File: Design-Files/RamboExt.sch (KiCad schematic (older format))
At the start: 44 parts, among them K1 SEL_THERM_4, K2 SEL_THERM_3, K3 MS3_E2, K4 MS2_E2, K5 MS1_E2, K6 MS3_E3, K7 MS2_E3, K8 MS1_E3, P1 STEPPER_2, P2 STEPPER_3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

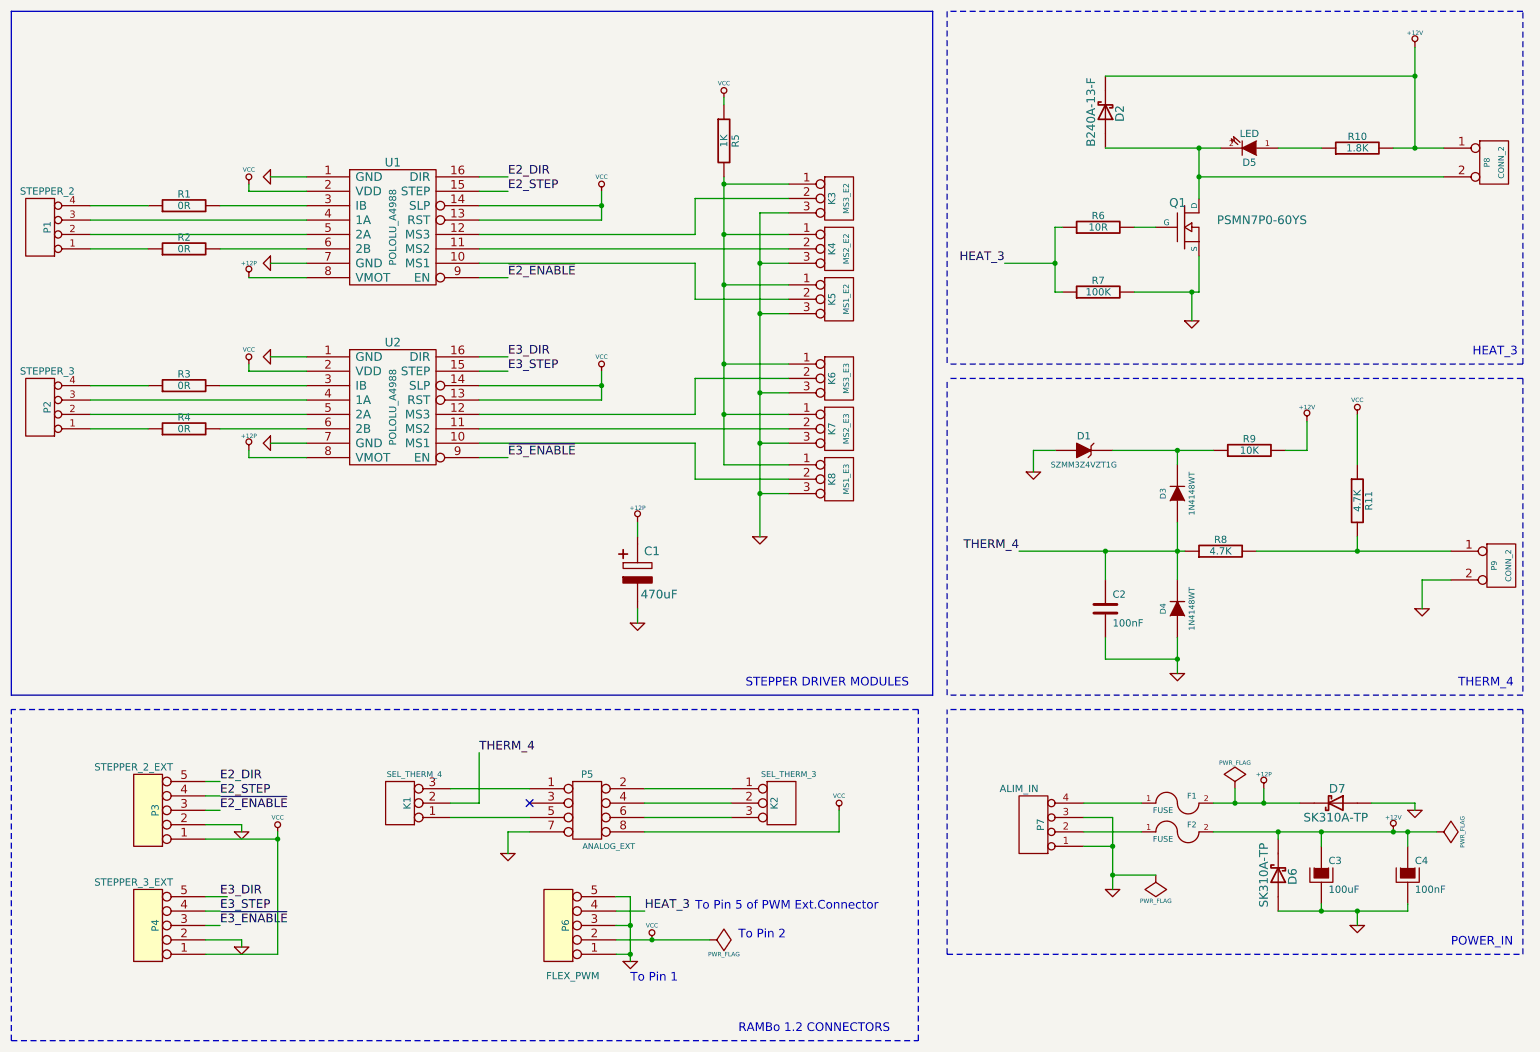
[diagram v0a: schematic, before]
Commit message: Adding PWM Connector. Since it is a separate board, the signal names change :
GND goes to GNDA
Vcc goes to Vdd.
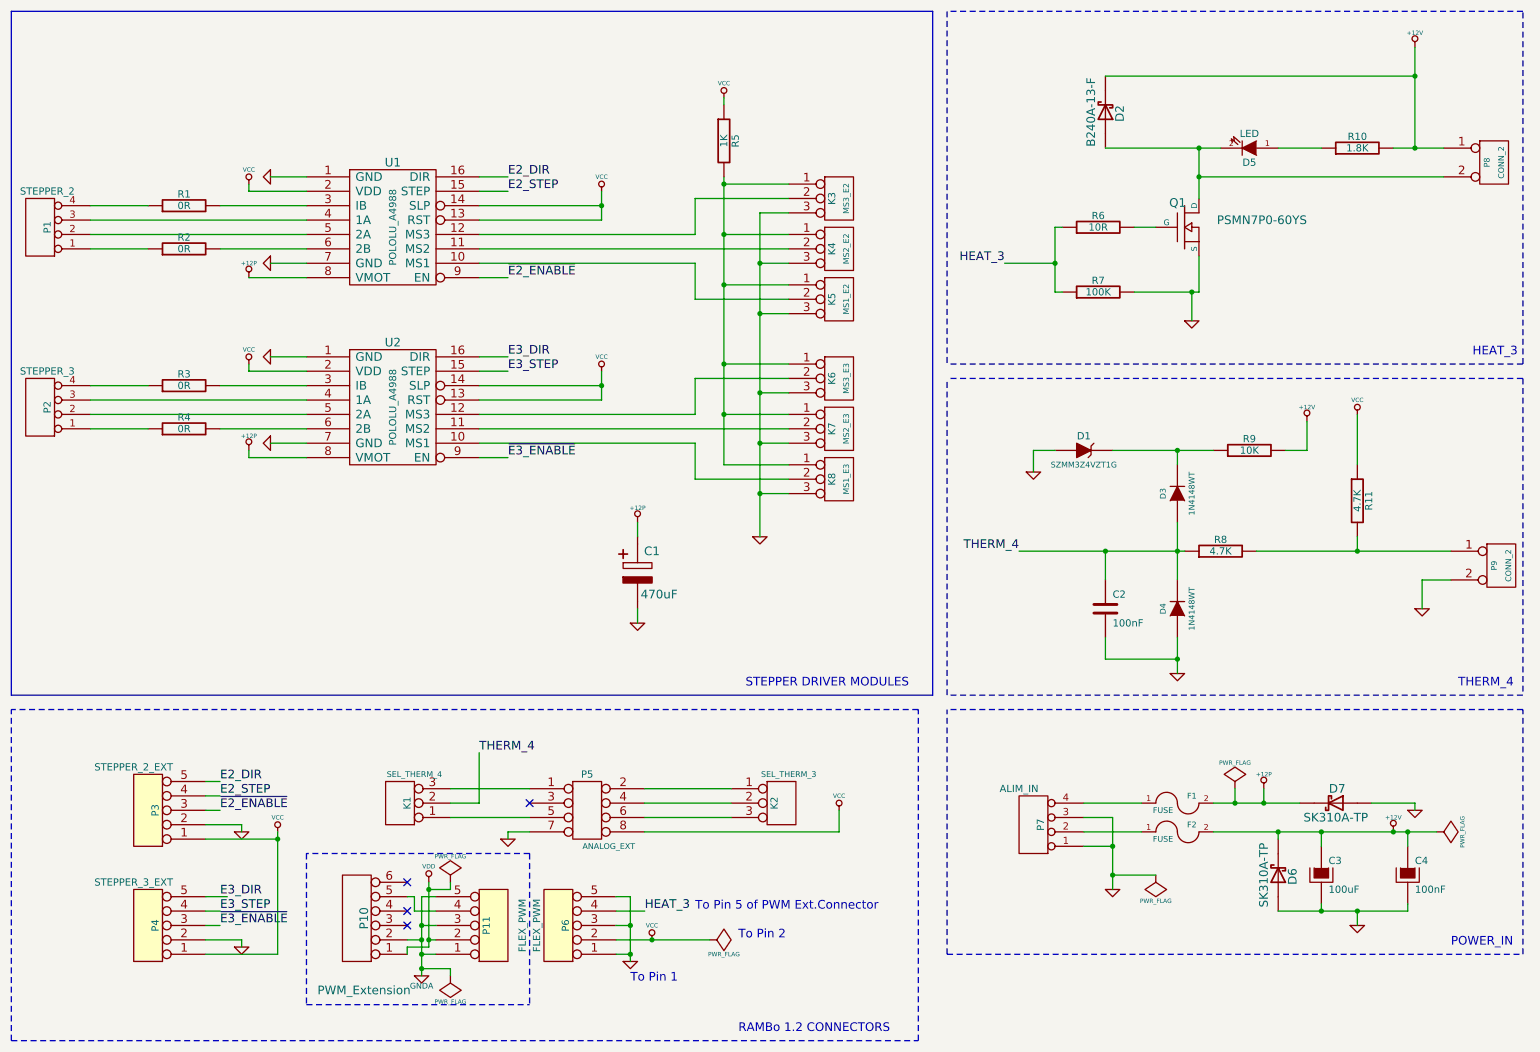
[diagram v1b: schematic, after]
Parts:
- added P10: PWM_Extension, symbol CONN_6
- added P11: FLEX_PWM, symbol CONN_5
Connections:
- new net: P10.5, P11.4
- new net GNDA: P10.2, P11.1, P11.3, P11.5
- new net VDD: P10.1, P11.2
- no-connect marks 1 -> 4
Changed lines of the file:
@@
 Sheet 1 1
 Title ""
-Date "25 mar 2014"
+Date "9 apr 2014"
 Rev ""
 Comp ""
@@
 Connection ~ 9750 6800
 Wire Wire Line
-	10350 6750 10350 6800
-Wire Wire Line
-	10350 6800 9450 6800
+	10350 6800 10350 6750
+Wire Wire Line
+	9450 6800 10350 6800
 Connection ~ 9750 6250
 Connection ~ 9450 6250
@@
 	9450 6250 9450 6300
 Wire Wire Line
-	9600 6050 9000 6050
+	9000 6050 9600 6050
 Wire Wire Line
 	10100 6050 10400 6050
@@
 Connection ~ 8300 6350
 Wire Wire Line
-	8300 6650 8300 6150
+	8300 6150 8300 6650
 Wire Wire Line
 	8300 6550 8600 6550
@@
 Connection ~ 8250 4300
 Wire Wire Line
-	8800 4300 7650 4300
+	7650 4300 8800 4300
 Wire Wire Line
 	10650 4500 10450 4500
@@
 	8250 4500 8250 4300
 Wire Wire Line
-	8750 5150 8750 4900
+	8750 4900 8750 5150
 Wire Wire Line
 	10000 3700 10000 3350
@@
 Connection ~ 10400 1500
 Wire Wire Line
-	10600 1500 10250 1500
+	10250 1500 10600 1500
 Connection ~ 8900 1500
 Wire Wire Line
@@
 	4250 6250 4100 6250
 Wire Wire Line
-	4100 6250 4100 6400
+	4100 6250 4100 6300
 Wire Notes Line
 	650  7700 650  5400
@@
 	9750 6800 9750 6750
 Wire Wire Line
-	10550 6250 9000 6250
+	9000 6250 10550 6250
 Connection ~ 10350 6250
 $Comp
@@
 L GND #PWR010
 U 1 1 53233AB5
-P 4100 6400
-F 0 "#PWR010" H 4100 6400 30  0001 C CNN
-F 1 "GND" H 4100 6330 30  0001 C CNN
-F 2 "" H 4100 6400 60  0001 C CNN
-F 3 "" H 4100 6400 60  0001 C CNN
-	1    4100 6400
+P 4100 6300
+F 0 "#PWR010" H 4100 6300 30  0001 C CNN
+F 1 "GND" H 4100 6230 30  0001 C CNN
+F 2 "" H 4100 6300 60  0001 C CNN
+F 3 "" H 4100 6300 60  0001 C CNN
+	1    4100 6300
 	1    0    0    -1
 $EndComp
@@
 $EndComp
 $Comp
-L GND #PWR?
+L GND #PWR037
 U 1 1 5331B0E0
 P 10000 6900
-F 0 "#PWR?" H 10000 6900 30  0001 C CNN
+F 0 "#PWR037" H 10000 6900 30  0001 C CNN
 F 1 "GND" H 10000 6830 30  0001 C CNN
 F 2 "" H 10000 6900 60  0000 C CNN
@@
 P 4450 6900
 F 0 "P6" V 4400 6900 50  0000 C CNN
-F 1 "FLEX_PWM" H 4350 7250 50  0000 C CNN
+F 1 "FLEX_PWM" V 4600 6900 50  0000 C CNN
 F 2 "" H 4450 6900 60  0000 C CNN
 F 3 "" H 4450 6900 60  0000 C CNN
@@
 Text Notes 4950 7300 0    60   ~ 0
 To Pin 1
+$Comp
+L CONN_5 P11
+U 1 1 53443222
+P 4000 6900
+F 0 "P11" V 3950 6900 50  0000 C CNN
+F 1 "FLEX_PWM" V 4200 6900 50  0000 C CNN
+F 2 "" H 4000 6900 60  0000 C CNN
+F 3 "" H 4000 6900 60  0000 C CNN
+	1    4000 6900
+	1    0    0    1
+$EndComp
+$Comp
+L CONN_6 P10
+U 1 1 53443248
+P 3050 6850
+F 0 "P10" V 3000 6850 60  0000 C CNN
+F 1 "PWM_Extension" H 3000 7350 60  0000 C CNN
+F 2 "" H 3050 6850 60  0000 C CNN
+F 3 "" H 3050 6850 60  0000 C CNN
+	1    3050 6850
+	-1   0    0    1
+$EndComp
+Wire Wire Line
+	3500 7100 3600 7100
+Wire Wire Line
+	3500 7000 3400 7000
+Wire Wire Line
+	3600 6900 3500 6900
+Connection ~ 3500 7000
+Wire Wire Line
+	3600 6700 3500 6700
+Connection ~ 3500 6900
+Wire Wire Line
+	3400 6700 3450 6700
+Wire Wire Line
+	3450 6700 3450 6800
+Wire Wire Line
+	3450 6800 3600 6800
+NoConn ~ 3400 6600
+NoConn ~ 3400 6800
+NoConn ~ 3400 6900
+Wire Notes Line
+	4250 6400 4250 7450
+Wire Notes Line
+	2700 7450 4250 7450
+Wire Notes Line
+	2700 6400 2700 7450
+Connection ~ 3500 7100
+$Comp
+L GNDA #PWR?
+U 1 1 534590D2
+P 3500 7250
+F 0 "#PWR?" H 3500 7250 40  0001 C CNN
+F 1 "GNDA" H 3500 7180 40  0000 C CNN
+F 2 "" H 3500 7250 60  0000 C CNN
+F 3 "" H 3500 7250 60  0000 C CNN
+	1    3500 7250
+	1    0    0    -1
+$EndComp
+$Comp
+L VDD #PWR?
+U 1 1 534590E1
+P 3550 6600
+F 0 "#PWR?" H 3550 6700 30  0001 C CNN
+F 1 "VDD" H 3550 6710 30  0000 C CNN
+F 2 "" H 3550 6600 60  0000 C CNN
+F 3 "" H 3550 6600 60  0000 C CNN
+	1    3550 6600
+	1    0    0    -1
+$EndComp
+$Comp
+L PWR_FLAG #FLG?
+U 1 1 534590F0
+P 3700 6600
+F 0 "#FLG?" H 3700 6695 30  0001 C CNN
+F 1 "PWR_FLAG" H 3700 6780 30  0000 C CNN
+F 2 "" H 3700 6600 60  0000 C CNN
+F 3 "" H 3700 6600 60  0000 C CNN
+	1    3700 6600
+	1    0    0    -1
+$EndComp
+$Comp
+L PWR_FLAG #FLG?
+U 1 1 534590FF
+P 3700 7250
+F 0 "#FLG?" H 3700 7345 30  0001 C CNN
+F 1 "PWR_FLAG" H 3700 7430 30  0000 C CNN
+F 2 "" H 3700 7250 60  0000 C CNN
+F 3 "" H 3700 7250 60  0000 C CNN
+	1    3700 7250
+	-1   0    0    1
+$EndComp
+Wire Wire Line
+	3500 6700 3500 7250
+Wire Wire Line
+	3500 7200 3700 7200
+Wire Wire Line
+	3700 7200 3700 7250
+Connection ~ 3500 7200
+Wire Wire Line
+	3400 7100 3400 7050
+Wire Wire Line
+	3400 7050 3550 7050
+Wire Wire Line
+	3550 7050 3550 6600
+Wire Wire Line
+	3700 6600 3700 6650
+Wire Wire Line
+	3700 6650 3550 6650
+Connection ~ 3550 6650
+Wire Wire Line
+	3600 7000 3550 7000
+Connection ~ 3550 7000
+Wire Notes Line
+	4250 6400 2700 6400
 $EndSCHEMATC

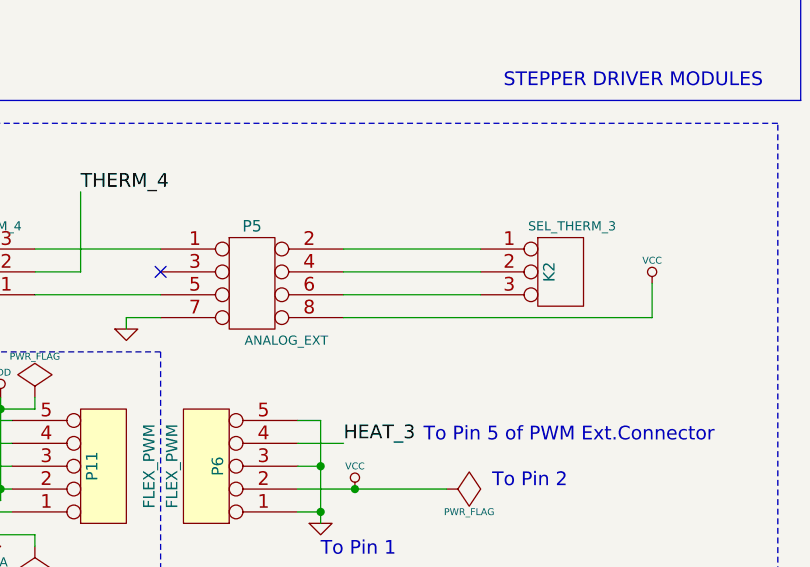
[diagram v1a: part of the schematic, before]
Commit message: Modifying Analog Extension Connector Pinning.
Removing selection of Therm3
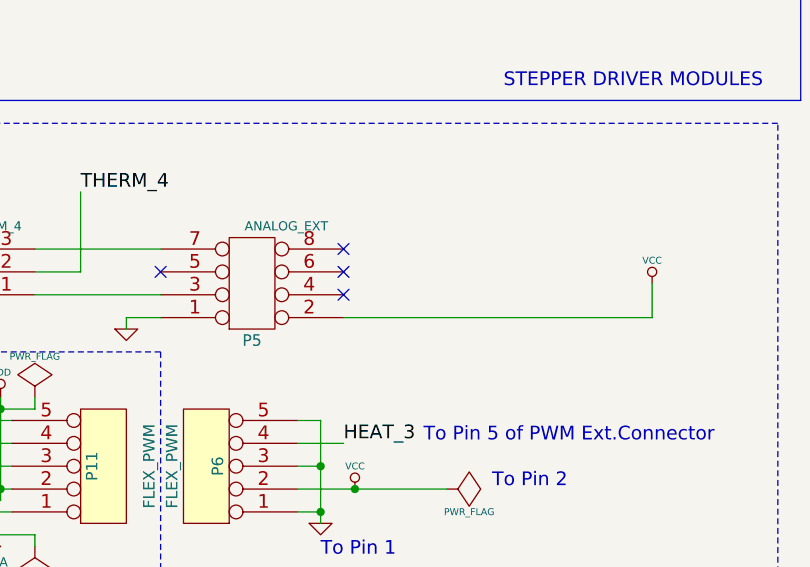
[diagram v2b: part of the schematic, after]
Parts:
- removed K2: SEL_THERM_3, symbol CONN_3
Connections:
- net GND: now also P5.1; no longer P5.7
- net VCC: now also P5.2; no longer P5.8
- net at K1.3 (P3): now also P5.7; no longer P5.1
- net at P5.3: now also K1.1 (P1)
- net at P5.5: no longer K1.1 (P1)
- no-connect marks 4 -> 7
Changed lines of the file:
@@
 Sheet 1 1
 Title ""
-Date "9 apr 2014"
+Date "14 apr 2014"
 Rev ""
 Comp ""
@@
 	4250 6150 3700 6150
 Wire Wire Line
-	5650 6150 5050 6150
-Wire Wire Line
-	5050 5950 5650 5950
-Wire Wire Line
 	2100 6900 2000 6900
 Wire Wire Line
@@
 	5600 1200 5600 1150
 Wire Wire Line
-	5050 6050 5650 6050
-Wire Wire Line
 	4250 5950 3700 5950
 Wire Wire Line
@@
 $EndComp
 $Comp
-L CONN_3 K2
-U 1 1 53233A2B
-P 6000 6050
-F 0 "K2" V 5950 6050 50  0000 C CNN
-F 1 "SEL_THERM_3" H 6050 6250 40  0000 C CNN
-F 2 "" H 6000 6050 60  0001 C CNN
-F 3 "" H 6000 6050 60  0001 C CNN
-	1    6000 6050
-	1    0    0    -1
-$EndComp
-$Comp
 L CONN_4X2 P5
 U 1 1 53233992
@@
 F 3 "" H 4650 6100 60  0001 C CNN
 	1    4650 6100
-	1    0    0    -1
+	1    0    0    1
 $EndComp
 $Comp
@@
 Wire Notes Line
 	4250 6400 2700 6400
+NoConn ~ 5050 5950
+NoConn ~ 5050 6050
+NoConn ~ 5050 6150
 $EndSCHEMATC
